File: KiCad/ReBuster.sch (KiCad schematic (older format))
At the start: 11 parts, among them U3 SN74CBTD16210, U4 SN74LVC16T245DGVR, U5 SN74CBTD16210, U6 SN74CBTD16210, U7 74LVC2T45DC, U8 PLCC_84_plug, U9 PLCC_84_plug

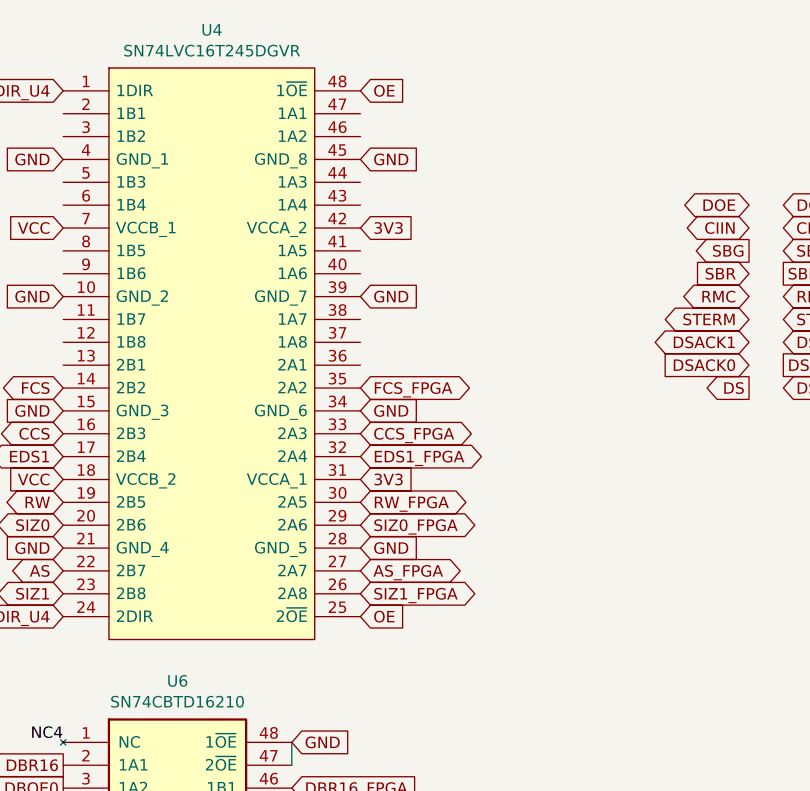
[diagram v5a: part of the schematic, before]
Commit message: Remove JP1 and assign its pull-up resistor to OE_U4
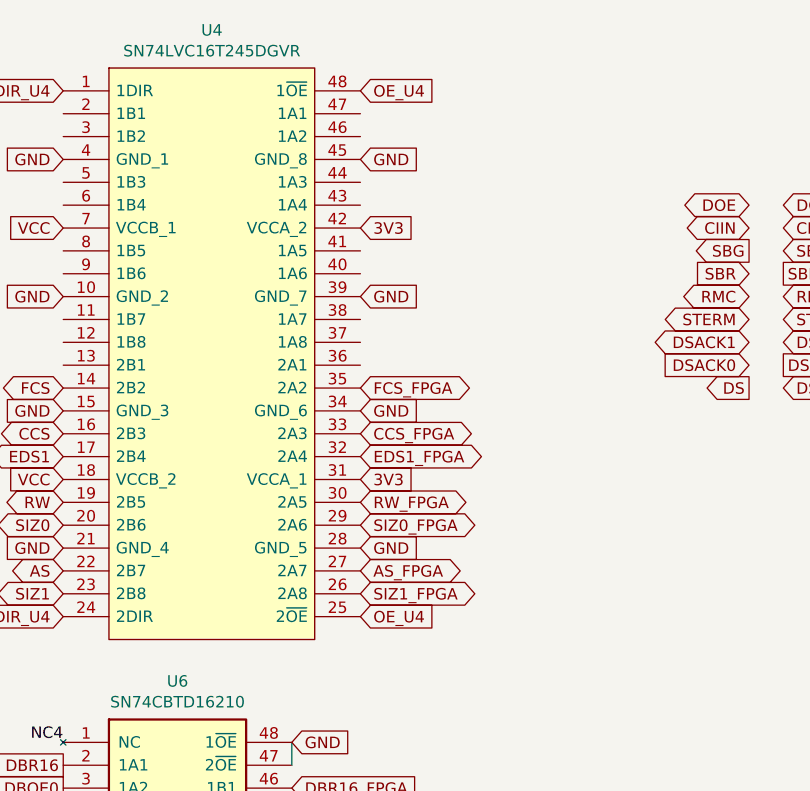
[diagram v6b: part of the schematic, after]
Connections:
- net OE renamed OE_U4
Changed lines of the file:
@@
 DIR_U4
 Text GLabel 10500 950  2    50   Input ~ 0
-OE
+OE_U4
 Text GLabel 10500 3250 2    50   Input ~ 0
-OE
+OE_U4
 Text GLabel 9200 2650 0    50   Input ~ 0
 VCC

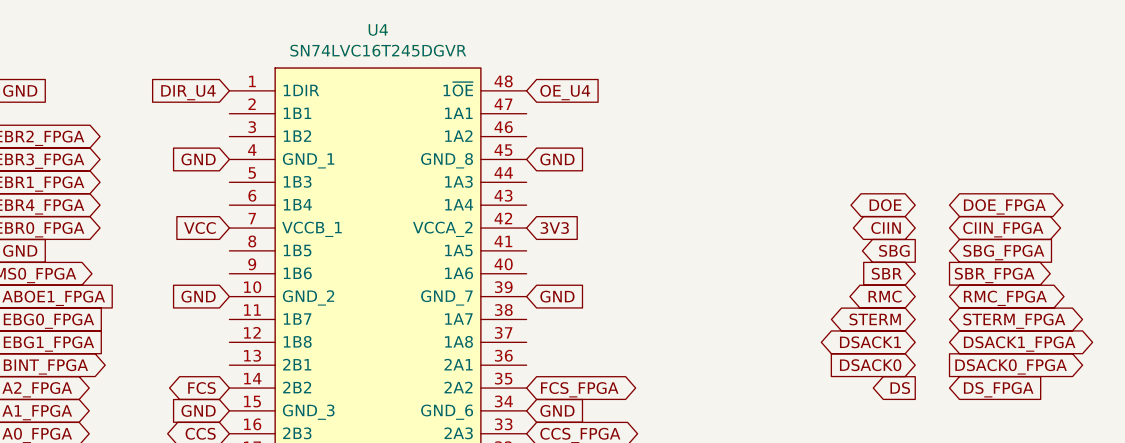
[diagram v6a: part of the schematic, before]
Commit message: Route DOE to U4 (SN74LVC16T245DGVR) change J1 -> M2 in FPGA
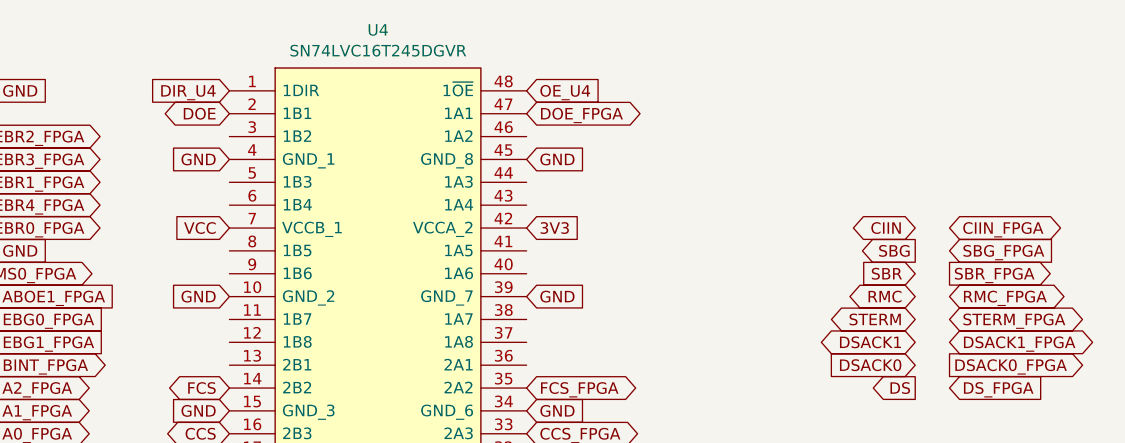
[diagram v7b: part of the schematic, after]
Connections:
- net DOE: now also U4.2 (1B1)
- net DOE_FPGA: now also U4.47 (1A1)
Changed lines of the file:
@@
 Text GLabel 10200 5200 2    50   Output ~ 0
 WAIT_FPGA
-Text GLabel 12350 1450 2    50   BiDi ~ 0
+Text GLabel 10500 1050 2    50   BiDi ~ 0
 DOE_FPGA
 Text GLabel 5650 6750 0    50   BiDi ~ 0
@@
 Text GLabel 6450 6750 2    50   BiDi ~ 0
 DTACK
-Text GLabel 12200 1450 0    50   BiDi ~ 0
+Text GLabel 9200 1050 0    50   BiDi ~ 0
 DOE
 Text GLabel 9200 5100 0    50   Input ~ 0

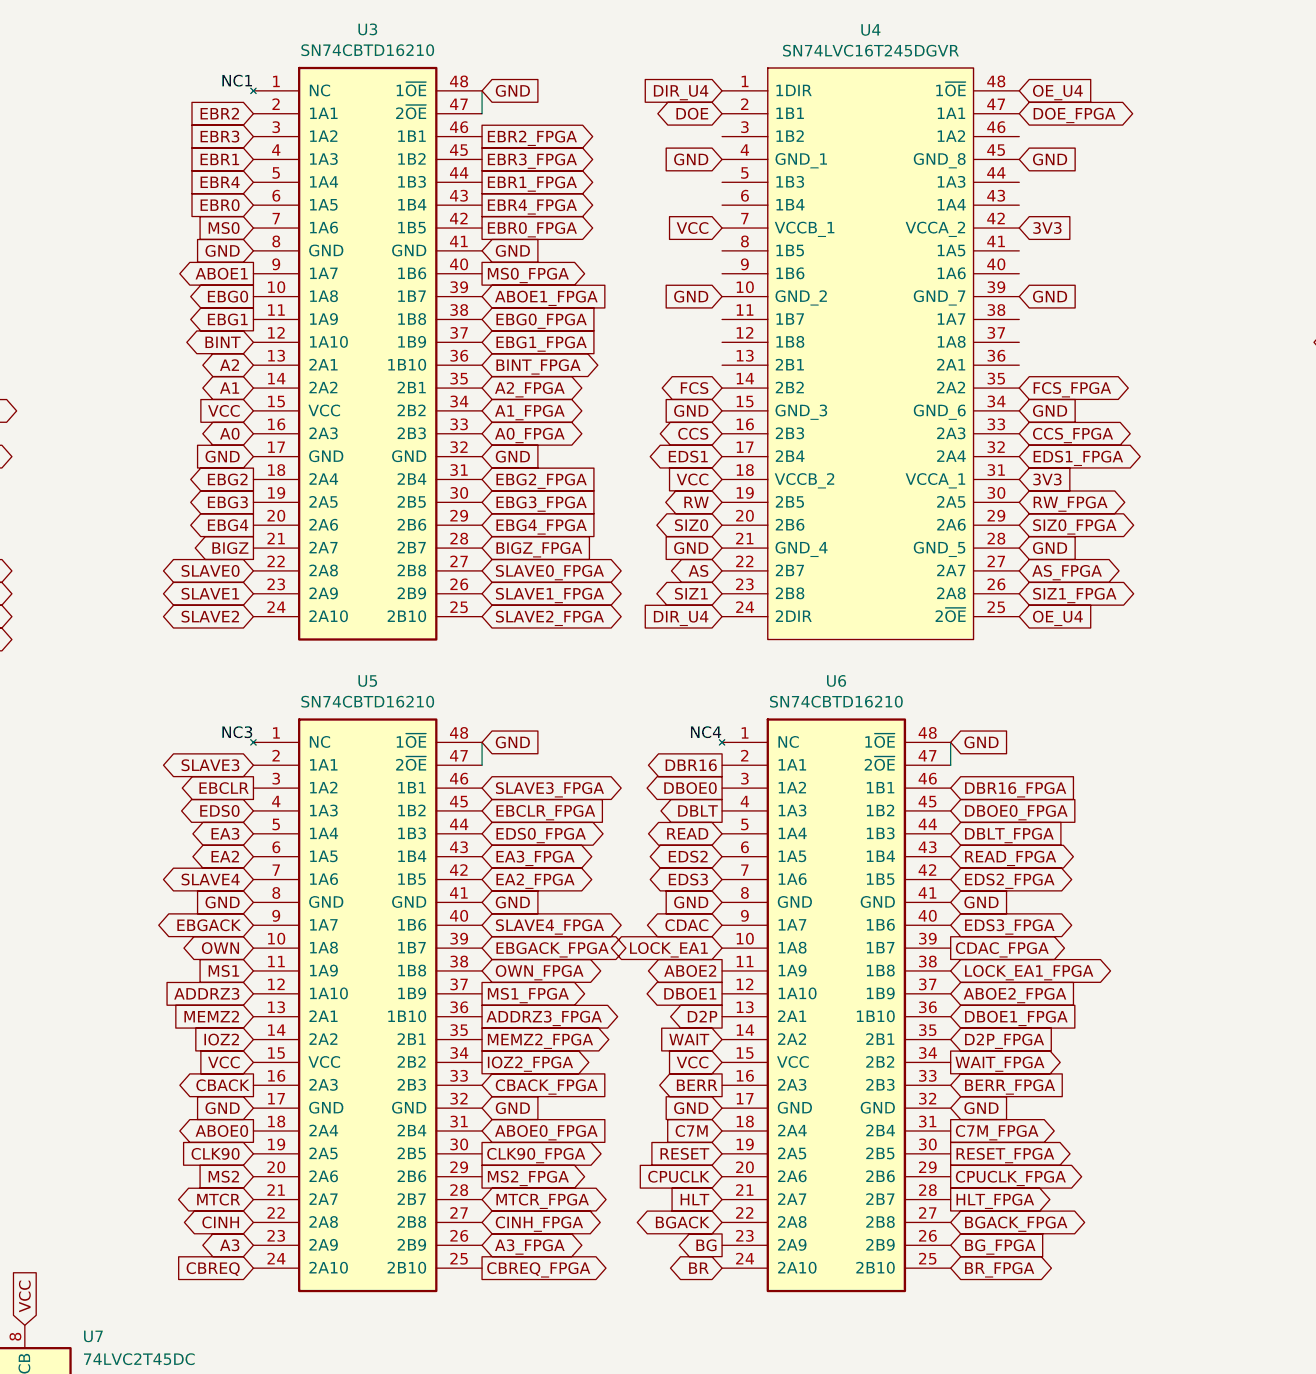
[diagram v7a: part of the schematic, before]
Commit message: Route READ to U4 (SN74LVC16T245DGVR) change H13 -> M1 in FPGA
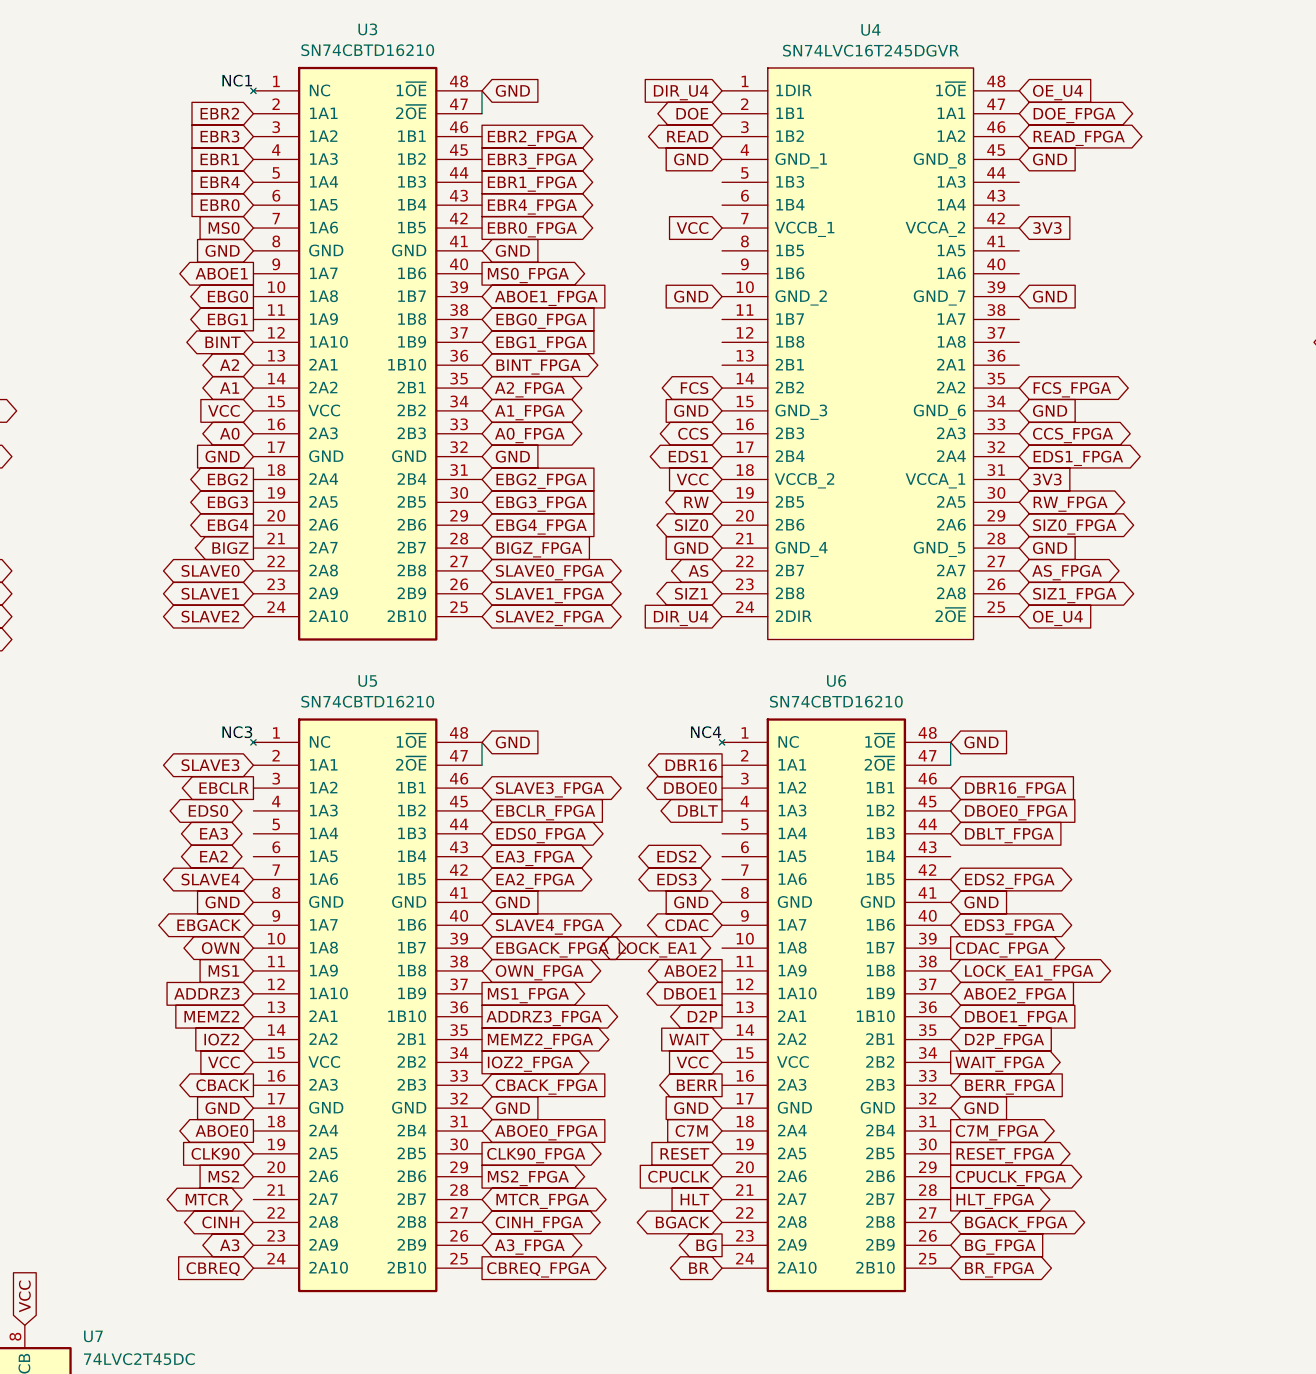
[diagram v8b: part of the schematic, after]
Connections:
- net EA2: no longer U5.6 (1A5)
- net EA3: no longer U5.5 (1A4)
- net EDS0: no longer U5.4 (1A3)
- net EDS2: no longer U6.6 (1A5)
- net EDS3: no longer U6.7 (1A6)
- net LOCK_EA1: no longer U6.10 (1A8)
- net MTCR: no longer U5.21 (2A7)
- net READ: now also U4.3 (1B2); no longer U6.5 (1A4)
- net READ_FPGA: now also U4.46 (1A2); no longer U6.43 (1B4)
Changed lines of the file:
@@
 Text GLabel 10200 4100 2    50   Input ~ 0
 DBOE0_FPGA
-Text GLabel 10200 4300 2    50   BiDi ~ 0
+Text GLabel 10500 1150 2    50   BiDi ~ 0
 READ_FPGA
 Text GLabel 10200 4400 2    50   BiDi ~ 0
@@
 Text GLabel 9200 4100 0    50   Output ~ 0
 DBLT
-Text GLabel 9200 4200 0    50   BiDi ~ 0
+Text GLabel 9200 1150 0    50   BiDi ~ 0
 READ
-Text GLabel 9200 4300 0    50   BiDi ~ 0
+Text GLabel 9150 4300 0    50   BiDi ~ 0
 EDS2
-Text GLabel 9200 4400 0    50   BiDi ~ 0
+Text GLabel 9150 4400 0    50   BiDi ~ 0
 EDS3
-Text GLabel 9200 4700 0    50   BiDi ~ 0
+Text GLabel 9150 4700 0    50   BiDi ~ 0
 LOCK_EA1
 Text GLabel 9200 4800 0    50   Output ~ 0
@@
 Text GLabel 7150 5700 0    50   Input ~ 0
 MS2
-Text GLabel 7150 5800 0    50   BiDi ~ 0
+Text GLabel 7100 5800 0    50   BiDi ~ 0
 MTCR
 Text GLabel 2750 4650 2    50   Output ~ 0
@@
 Text GLabel 7150 4400 0    50   BiDi ~ 0
 SLAVE4
-Text GLabel 7150 4300 0    50   BiDi ~ 0
+Text GLabel 7100 4300 0    50   BiDi ~ 0
 EA2
-Text GLabel 7150 4200 0    50   BiDi ~ 0
+Text GLabel 7100 4200 0    50   BiDi ~ 0
 EA3
 Text GLabel 9200 2550 0    50   BiDi ~ 0
@@
 Text GLabel 2750 2850 2    50   BiDi ~ 0
 EDS0
-Text GLabel 7150 4100 0    50   BiDi ~ 0
+Text GLabel 7100 4100 0    50   BiDi ~ 0
 EDS0
 $Comp
